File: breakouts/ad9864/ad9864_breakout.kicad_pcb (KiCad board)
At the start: 2 copper layers, 164 parts, among them P101 CONN_01X02, P102 CONN_01X08, P103 CONN_02X08, U101 CONN_SMA, U102 CONN_SMA, U103 ad9864, U104 TXCO, U105 CONN_SMA, U106 CONN_SMA, U107 max2605

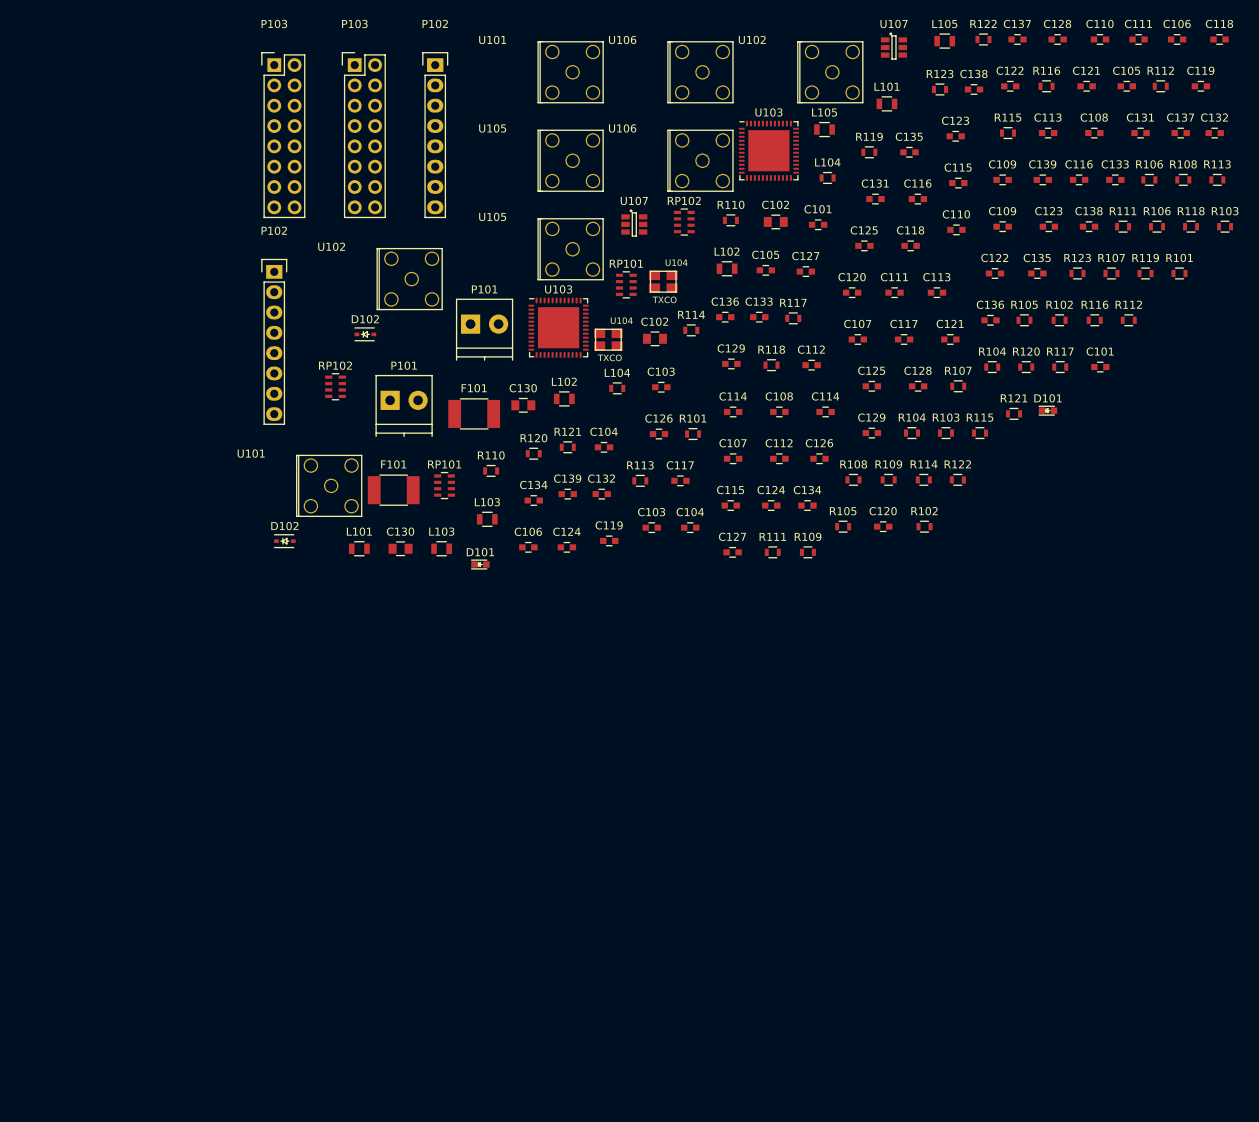
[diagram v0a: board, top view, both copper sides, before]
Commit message: started on synth r1 (fixed r0 bugs..), component placement on ad9864 breakout
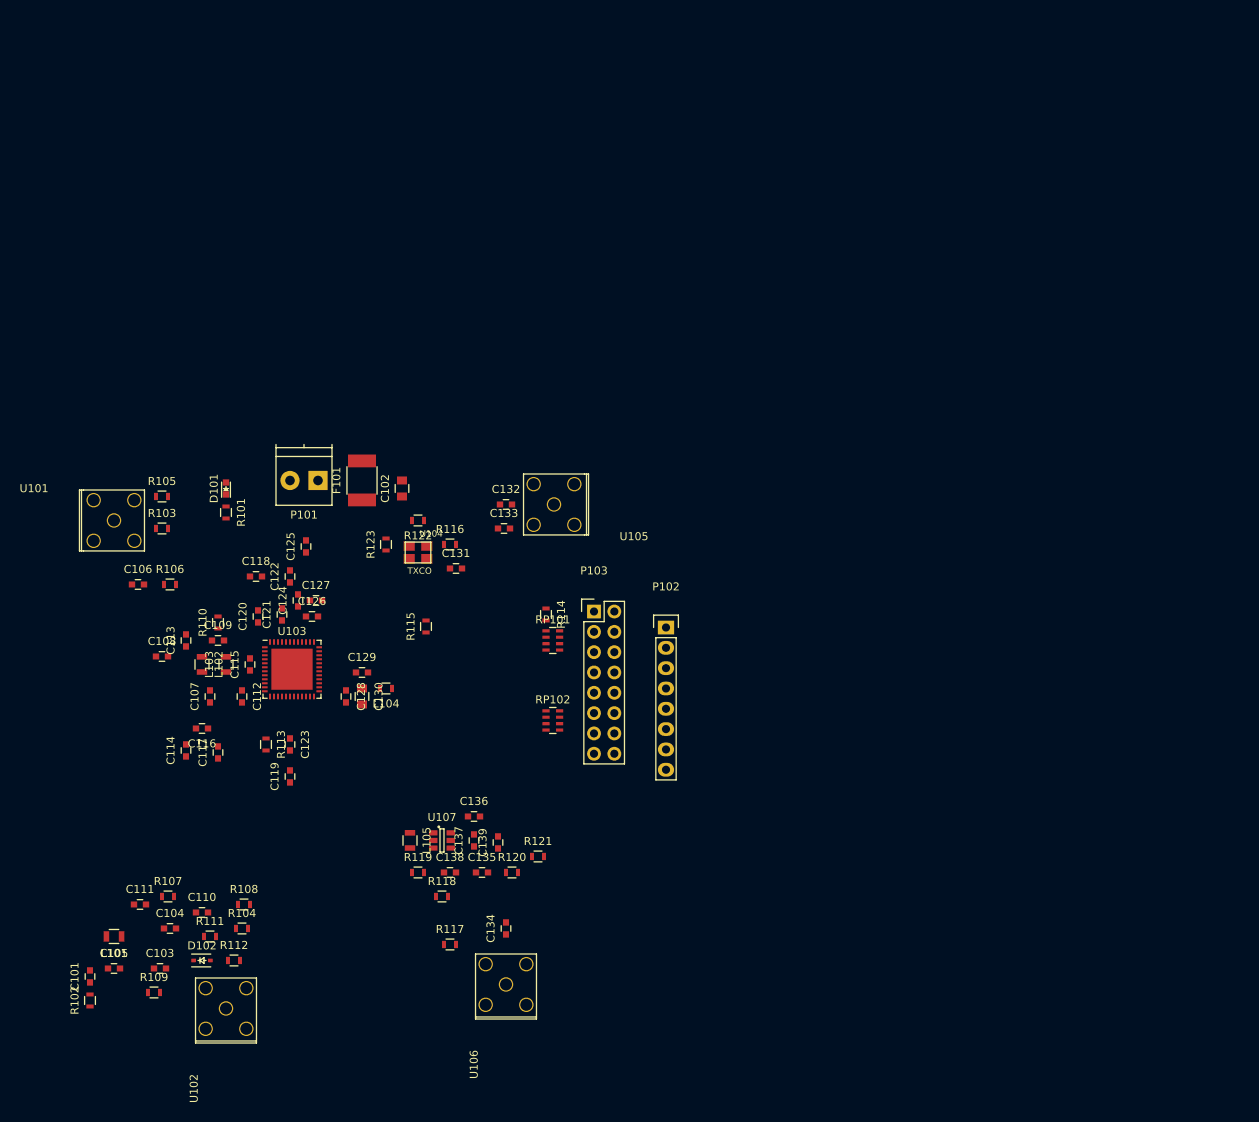
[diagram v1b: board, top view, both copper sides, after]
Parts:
- removed the C101 at (197.0, 54.0)
- removed the C101 at (232.3, 71.8)
- removed the C102 at (176.6, 68.3)
- removed the C102 at (191.7, 53.7)
- removed the C103 at (177.4, 74.3)
- removed the C103 at (176.2, 91.9)
- removed the C104 at (170.3, 81.9)
- removed the C104 at (181.0, 91.9)
- removed the C105 at (190.5, 59.7)
- removed the C105 at (235.6, 36.7)
- removed the C106 at (160.8, 94.4)
- removed the C106 at (241.9, 30.9)
- removed the C107 at (186.4, 83.3)
- removed the C107 at (202.0, 68.4)
- removed the C108 at (192.2, 77.4)
- removed the C108 at (231.5, 42.6)
- removed the C109 at (220.1, 48.4)
- removed the C109 at (220.1, 54.3)
- removed the C110 at (232.3, 30.9)
- removed the C110 at (214.3, 54.7)
- removed the C111 at (237.1, 30.9)
- removed the C111 at (206.6, 62.5)
- removed the C112 at (196.2, 71.6)
- removed the C112 at (192.2, 83.3)
- removed the C113 at (225.8, 42.6)
- removed the C113 at (211.9, 62.5)
- removed the C114 at (186.4, 77.4)
- removed the C114 at (198.0, 77.4)
- removed the C115 at (214.5, 48.8)
- removed the C115 at (186.1, 89.1)
- removed the C116 at (209.5, 50.8)
- removed the C116 at (229.6, 48.4)
- removed the C117 at (179.8, 86.0)
- removed the C117 at (207.8, 68.4)
- removed the C118 at (208.6, 56.7)
- removed the C118 at (247.2, 30.9)
- removed the C119 at (170.9, 93.6)
- removed the C119 at (244.9, 36.7)
- removed the C120 at (201.3, 62.5)
- removed the C120 at (205.2, 91.8)
- removed the C121 at (230.6, 36.7)
- removed the C121 at (213.5, 68.4)
- removed the C122 at (221.0, 36.7)
- removed the C122 at (219.1, 60.1)
- removed the C123 at (214.2, 43.0)
- removed the C123 at (225.9, 54.3)
- removed the C124 at (165.6, 94.4)
- removed the C124 at (191.2, 89.1)
- removed the C125 at (202.8, 56.7)
- removed the C125 at (203.7, 74.2)
- removed the C126 at (177.1, 80.2)
- removed the C126 at (197.2, 83.3)
- removed the C127 at (195.5, 59.9)
- removed the C127 at (186.3, 95.0)
- removed the C128 at (227.0, 30.9)
- removed the C128 at (209.5, 74.2)
- removed the C129 at (186.2, 71.4)
- removed the C129 at (203.7, 80.1)
- removed the C130 at (160.2, 76.6)
- removed the C130 at (144.8, 94.5)
- removed the C131 at (204.2, 50.8)
- removed the C131 at (237.3, 42.6)
- removed the C132 at (170.0, 87.7)
- removed the C132 at (246.6, 42.6)
- removed the C133 at (189.7, 65.6)
- removed the C133 at (234.2, 48.4)
- removed the C134 at (161.5, 88.5)
- removed the C134 at (195.7, 89.1)
- removed the C135 at (208.4, 45.0)
- removed the C135 at (224.4, 60.1)
- removed the C136 at (185.4, 65.6)
- removed the C136 at (218.6, 66.0)
- removed the C137 at (221.9, 30.9)
- removed the C137 at (242.3, 42.6)
- removed the C138 at (216.5, 37.1)
- removed the C138 at (230.9, 54.3)
- removed the C139 at (165.7, 87.7)
- removed the C139 at (225.1, 48.4)
- removed the D101 at (225.7, 77.3)
- removed the D101 at (154.8, 96.5)
- removed the D102 at (130.4, 93.6)
- removed the D102 at (140.4, 67.7)
- removed the F101 at (154.0, 77.7)
- removed the F101 at (144.0, 87.2)
- removed the L101 at (139.7, 94.5)
- removed the L101 at (205.6, 38.9)
- removed the L102 at (185.6, 59.5)
- removed the L102 at (165.3, 75.8)
- removed the L103 at (155.7, 90.9)
- removed the L103 at (150.0, 94.5)
- removed the L104 at (198.2, 48.2)
- removed the L104 at (171.9, 74.5)
- removed the L105 at (197.8, 42.1)
- removed the L105 at (212.8, 31.1)
- removed the P101 at (143.5, 76.0)
- removed the P101 at (153.6, 66.5)
- removed the P102 at (149.2, 34.1)
- removed the P102 at (129.0, 59.9)
- removed the P103 at (129.0, 34.1)
- removed the P103 at (139.1, 34.1)
- removed the R101 at (181.4, 80.2)
- removed the R101 at (242.2, 60.1)
- removed the R102 at (227.2, 66.0)
- removed the R102 at (210.3, 91.8)
- removed the R103 at (213.0, 80.1)
- removed the R103 at (247.9, 54.3)
- removed the R104 at (218.8, 71.8)
- removed the R104 at (208.7, 80.1)
- removed the R105 at (200.1, 91.8)
- removed the R105 at (222.8, 66.0)
- removed the R106 at (239.4, 54.3)
- removed the R106 at (238.4, 48.4)
- removed the R107 at (233.7, 60.1)
- removed the R107 at (214.5, 74.2)
- removed the R108 at (242.7, 48.4)
- removed the R108 at (201.4, 85.9)
- removed the R109 at (205.8, 85.9)
- removed the R109 at (195.7, 95.0)
- removed the R110 at (156.1, 84.8)
- removed the R110 at (186.1, 53.5)
- removed the R111 at (191.3, 95.0)
- removed the R111 at (235.1, 54.3)
- removed the R112 at (239.8, 36.7)
- removed the R112 at (235.8, 66.0)
- removed the R113 at (174.8, 86.0)
- removed the R113 at (246.9, 48.4)
- removed the R114 at (181.2, 67.2)
- removed the R114 at (210.2, 85.9)
- removed the R115 at (220.7, 42.6)
- removed the R115 at (217.2, 80.1)
- removed the R116 at (225.6, 36.7)
- removed the R116 at (231.6, 66.0)
- removed the R117 at (193.9, 65.7)
- removed the R117 at (227.3, 71.8)
- removed the R118 at (191.2, 71.6)
- removed the R118 at (243.6, 54.3)
- removed the R119 at (203.4, 45.0)
- removed the R119 at (237.9, 60.1)
- removed the R120 at (161.5, 82.7)
- removed the R120 at (223.0, 71.8)
- removed the R121 at (165.7, 81.9)
- removed the R121 at (221.5, 77.7)
- removed the R122 at (217.7, 30.9)
- removed the R122 at (214.5, 85.9)
- removed the R123 at (212.2, 37.1)
- removed the R123 at (229.4, 60.1)
- removed the RP101 at (150.3, 86.6)
- removed the RP101 at (173.0, 61.5)
- removed the RP102 at (136.7, 74.3)
- removed the RP102 at (180.3, 53.7)
- removed the U101 at (136.2, 86.7)
- removed the U101 at (166.3, 35.0)
- removed the U102 at (198.8, 35.0)
- removed the U102 at (146.2, 60.8)
- removed the U103 at (164.6, 66.9)
- removed the U103 at (190.9, 44.8)
- removed the U104 at (170.8, 68.4)
- removed the U104 at (177.7, 61.2)
- removed the U105 at (166.3, 57.1)
- removed the U105 at (166.3, 46.0)
- removed the U106 at (182.6, 46.0)
- removed the U106 at (182.6, 35.0)
- removed the U107 at (206.5, 31.9)
- removed the U107 at (174.0, 54.0)
- added C101: 330 pF, Capacitors_SMD:C_0603, F.Cu at (106.0, 148.0)
- added C102: 10 uF, Capacitors_SMD:C_0805, F.Cu at (145.0, 87.0)
- added C103: 10 nF, Capacitors_SMD:C_0603, F.Cu at (114.8, 147.0)
- added C104: 10 nF, Capacitors_SMD:C_0603, F.Cu at (116.0, 142.0)
- added C105: DNP, Capacitors_SMD:C_0603, F.Cu at (109.0, 147.0)
- added C106: 10 nF, Capacitors_SMD:C_0603, F.Cu at (112.0, 99.0)
- added C107: 100 nF, Capacitors_SMD:C_0603, F.Cu at (121.0, 113.0)
- added C108: 100 pF, Capacitors_SMD:C_0603, F.Cu at (115.0, 108.0)
- added C109: 180 pF, Capacitors_SMD:C_0603, F.Cu at (122.0, 106.0)
- added C110: 10 nF, Capacitors_SMD:C_0603, F.Cu at (120.0, 140.0)
- added C111: 10 nF, Capacitors_SMD:C_0603, F.Cu at (112.2, 139.0)
- added C112: 100 nF, Capacitors_SMD:C_0603, F.Cu at (125.0, 113.0)
- added C113: 100 pF, Capacitors_SMD:C_0603, F.Cu at (118.0, 106.0)
- added C114: 100 pF, Capacitors_SMD:C_0603, F.Cu at (118.0, 119.8)
- added C115: 2.2 nF, Capacitors_SMD:C_0603, F.Cu at (126.0, 109.0)
- added C116: 10 nF, Capacitors_SMD:C_0603, F.Cu at (120.0, 117.0)
- added C117: 100 pF, Capacitors_SMD:C_0603, F.Cu at (122.0, 120.0)
- added C118: 100 nF, Capacitors_SMD:C_0603, F.Cu at (126.8, 98.0)
- added C119: 100 nF, Capacitors_SMD:C_0603, F.Cu at (131.0, 123.0)
- added C120: 100 nF, Capacitors_SMD:C_0603, F.Cu at (127.0, 103.0)
- added C121: 100 nF, Capacitors_SMD:C_0603, F.Cu at (130.0, 102.8)
- added C122: 10 nF, Capacitors_SMD:C_0603, F.Cu at (131.0, 98.0)
- added C123: 100 nF, Capacitors_SMD:C_0603, F.Cu at (131.0, 119.0)
- added C124: 10 nF, Capacitors_SMD:C_0603, F.Cu at (132.0, 101.0)
- added C125: 100 nF, Capacitors_SMD:C_0603, F.Cu at (133.0, 94.2)
- added C126: 1 nF, Capacitors_SMD:C_0603, F.Cu at (133.8, 103.0)
- added C127: 100 nF, Capacitors_SMD:C_0603, F.Cu at (134.2, 101.0)
- added C128: 100 nF, Capacitors_SMD:C_0603, F.Cu at (138.0, 113.0)
- added C129: 100 nF, Capacitors_SMD:C_0603, F.Cu at (140.0, 110.0)
- added C130: 10 uF, Capacitors_SMD:C_0805, F.Cu at (140.0, 113.0)
- added C131: 100 nF, Capacitors_SMD:C_0603, F.Cu at (151.8, 97.0)
- added C132: DNP, Capacitors_SMD:C_0603, F.Cu at (158.0, 89.0)
- added C133: DNP, Capacitors_SMD:C_0603, F.Cu at (157.8, 92.0)
- added C134: DNP, Capacitors_SMD:C_0603, F.Cu at (158.0, 142.0)
- added C135: 100 nF, Capacitors_SMD:C_0603, F.Cu at (155.0, 135.0)
- added C136: 1 nF, Capacitors_SMD:C_0603, F.Cu at (154.0, 128.0)
- added C137: TBD, Capacitors_SMD:C_0603, F.Cu at (154.0, 131.0)
- added C138: TBD, Capacitors_SMD:C_0603, F.Cu at (151.0, 135.0)
- added C139: TBD, Capacitors_SMD:C_0603, F.Cu at (157.0, 131.2)
- added D101: LED, LEDs:LED_0603, F.Cu at (123.0, 87.0)
- added D102: SMV1702-011LF, Diodes_SMD:SOD-323, F.Cu at (120.0, 146.0)
- added F101: F_Small, Resistors_SMD:R_1812, F.Cu at (140.0, 86.0)
- added L101: 1.2 uH, Resistors_SMD:R_0805, F.Cu at (109.0, 143.0)
- added L102: 10 mH, Resistors_SMD:R_0805, F.Cu at (120.0, 109.0)
- added L103: 10 mH, Resistors_SMD:R_0805, F.Cu at (123.0, 109.0)
- added L104: L_Small, Resistors_SMD:R_0603, F.Cu at (143.0, 112.0)
- added L105: 10 mH, Resistors_SMD:R_0805, F.Cu at (146.0, 131.0)
- added P101: CONN_01X02, Terminal_Blocks:TerminalBlock_Pheonix_PT-3.5mm_2pol, F.Cu at (134.5, 86.0)
- added P102: CONN_01X08, Pin_Headers:Pin_Header_Straight_1x08, F.Cu at (178.0, 104.4)
- added P103: CONN_02X08, Pin_Headers:Pin_Header_Straight_2x08, F.Cu at (169.0, 102.4)
- added R101: 1k, Resistors_SMD:R_0603, F.Cu at (123.0, 90.0)
- added R102: 28.7k, Resistors_SMD:R_0603, F.Cu at (106.0, 151.0)
- added R103: DNP, Resistors_SMD:R_0603, F.Cu at (115.0, 92.0)
- added R104: 10k, Resistors_SMD:R_0603, F.Cu at (125.0, 142.0)
- added R105: 0, Resistors_SMD:R_0603, F.Cu at (115.0, 88.0)
- added R106: 57.6, Resistors_SMD:R_0603, F.Cu at (116.0, 99.0)
- added R107: 0, Resistors_SMD:R_0603, F.Cu at (115.8, 138.0)
- added R108: 0, Resistors_SMD:R_0603, F.Cu at (125.2, 139.0)
- added R109: 2.87k, Resistors_SMD:R_0603, F.Cu at (114.0, 150.0)
- added R110: R_Small, Resistors_SMD:R_0603, F.Cu at (122.0, 103.8)
- added R111: DNP, Resistors_SMD:R_0603, F.Cu at (121.0, 143.0)
- added R112: 51, Resistors_SMD:R_0603, F.Cu at (124.0, 146.0)
- added R113: 100k, Resistors_SMD:R_0603, F.Cu at (128.0, 119.0)
- added R114: 1k, Resistors_SMD:R_0603, F.Cu at (163.0, 102.8)
- added R115: DNP, Resistors_SMD:R_0603, F.Cu at (148.0, 104.2)
- added R116: 0, Resistors_SMD:R_0603, F.Cu at (151.0, 94.0)
- added R117: DNP, Resistors_SMD:R_0603, F.Cu at (151.0, 144.0)
- added R118: 0, Resistors_SMD:R_0603, F.Cu at (150.0, 138.0)
- added R119: 0, Resistors_SMD:R_0603, F.Cu at (147.0, 135.0)
- added R120: DNP, Resistors_SMD:R_0603, F.Cu at (158.8, 135.0)
- added R121: TBD, Resistors_SMD:R_0603, F.Cu at (162.0, 133.0)
- added R122: 1k, Resistors_SMD:R_0603, F.Cu at (147.0, 91.0)
- added R123: DNP, Resistors_SMD:R_0603, F.Cu at (143.0, 94.0)
- added RP101: 22, Resistors_SMD:R_Array_Concave_4x0603, F.Cu at (163.8, 106.0)
- added RP102: 22, Resistors_SMD:R_Array_Concave_4x0603, F.Cu at (163.8, 116.0)
- added U101: CONN_SMA, vna_footprints:732512200_SMA, F.Cu at (109.0, 91.0)
- added U102: CONN_SMA, vna_footprints:732512200_SMA, F.Cu at (123.0, 152.0)
- added U103: ad9864, Housings_DFN_QFN:QFN-48-1EP_7x7mm_Pitch0.5mm, F.Cu at (131.2, 109.6)
- added U104: TXCO, vna_footprints:crystal_FA238-TSX3225, F.Cu at (147.0, 95.0)
- added U105: CONN_SMA, vna_footprints:732512200_SMA, F.Cu at (164.0, 89.0)
- added U106: CONN_SMA, vna_footprints:732512200_SMA, F.Cu at (158.0, 149.0)
- added U107: max2605, TO_SOT_Packages_SMD:SOT-23-6, F.Cu at (150.0, 131.0)
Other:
- net class Default: clearance 0.2 -> 0.14
- rule trace_clearance: 0.2 -> 0.14

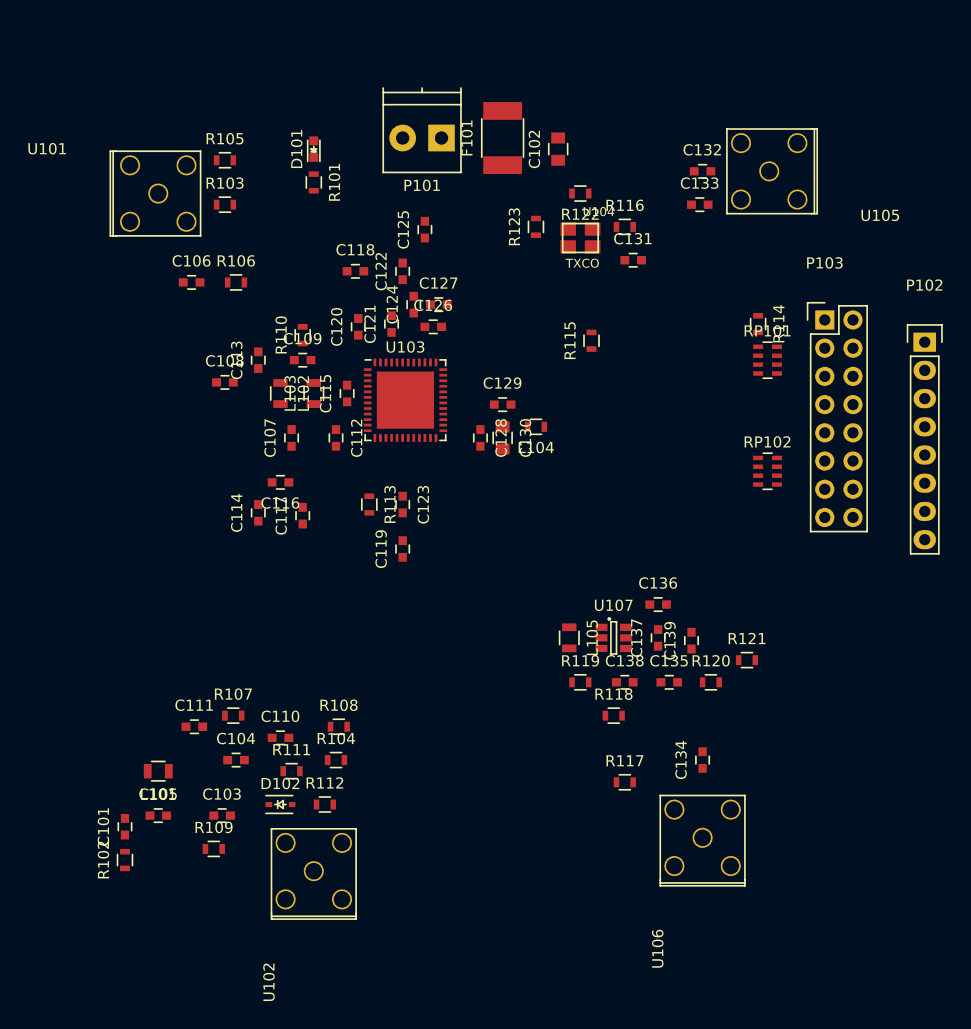
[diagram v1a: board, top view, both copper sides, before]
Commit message: component placement on ad9864 breakout
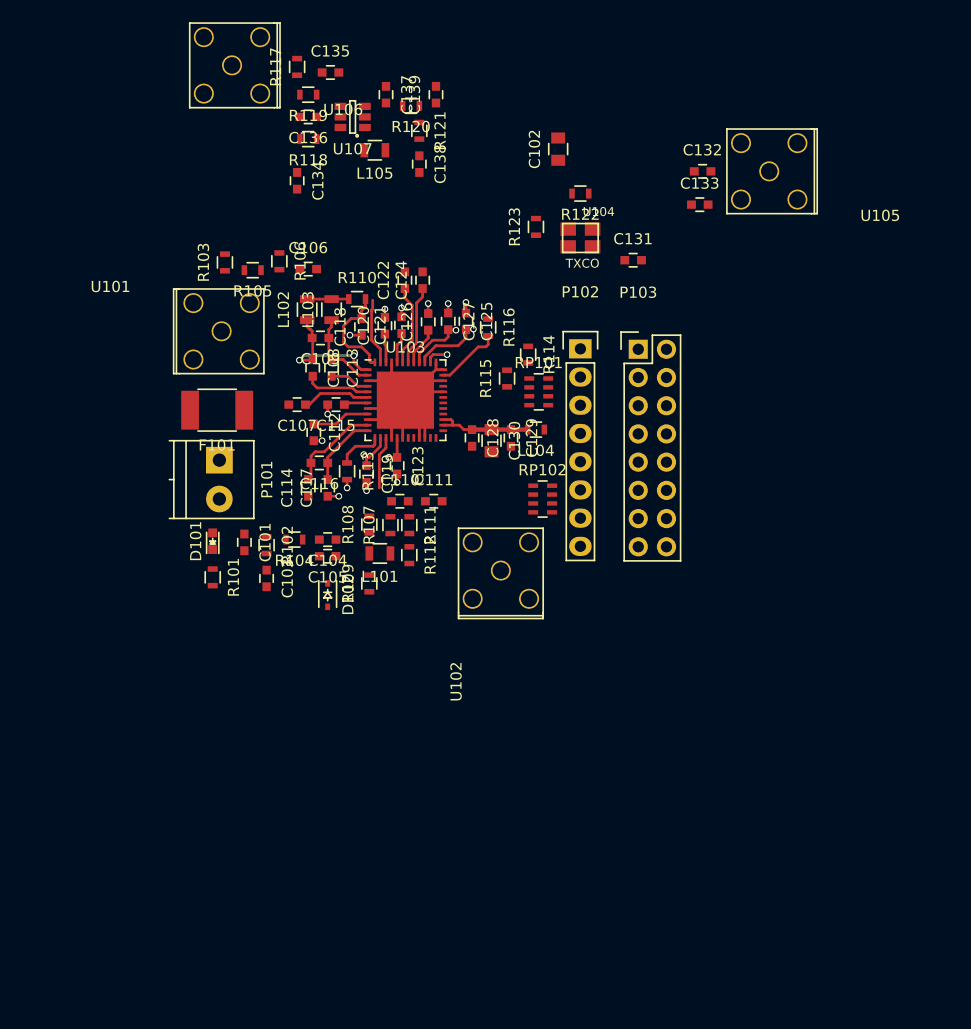
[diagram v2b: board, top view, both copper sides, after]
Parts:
- L102, L103, L105: value 10 mH -> 10 uH
- moved U106 81.4 mm to (115.6, 79.5), turned to 180 degrees
- moved R117 70.8 mm to (121.5, 79.6), turned to 90 degrees
- moved C134 63.7 mm to (121.5, 89.8), turned to 270 degrees
- moved C135 62.8 mm to (124.5, 80.1)
- moved R118 58.7 mm to (122.5, 86.1), turned to 180 degrees
- moved R120 58.5 mm to (131.8, 83.1), turned to 180 degrees
- moved R119 58.3 mm to (122.5, 82.1), turned to 180 degrees
- moved R121 56.0 mm to (132.5, 85.3), turned to 270 degrees
- moved C137 54.7 mm to (129.5, 82.1), turned to 270 degrees
- moved C139 54.3 mm to (134.0, 82.1)
- moved C136 54.0 mm to (122.5, 84.1), turned to 180 degrees
- moved U107 52.5 mm to (126.5, 84.1), turned to 180 degrees
- moved C138 50.2 mm to (132.5, 88.3), turned to 270 degrees
- moved L105 47.3 mm to (128.5, 87.1), turned to 180 degrees
- moved R101 36.7 mm to (113.9, 125.5)
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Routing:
- net +3V3: track 0.00 -> 38.6 mm, vias 0 -> 4
- net GND: track 0.00 -> 29.9 mm, vias 0 -> 12
- net Net-(C108-Pad1): track 0.00 -> 12.2 mm, vias 0 -> 2
- net Net-(C128-Pad1): track 0.00 -> 9.03 mm
- net Net-(C114-Pad2): track 0.00 -> 8.48 mm
- net Net-(C109-Pad1): track 0.00 -> 7.59 mm
- net Net-(C122-Pad1): track 0.00 -> 7.28 mm
- net Net-(C124-Pad1): track 0.00 -> 7.19 mm
- net Net-(C116-Pad1): track 0.00 -> 6.59 mm
- net Net-(C132-Pad1): track 0.00 -> 5.99 mm
- net /IFIN: track 0.00 -> 5.97 mm
- net Net-(C108-Pad2): track 0.00 -> 5.94 mm
- net /IOUTC: track 0.00 -> 4.75 mm
- net Net-(R113-Pad1): track 0.00 -> 4.22 mm
- net Net-(L102-Pad2): track 0.00 -> 3.75 mm
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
